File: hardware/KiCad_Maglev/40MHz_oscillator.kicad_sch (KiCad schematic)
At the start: 4 parts, among them Y2 IQXC-42_830108213209

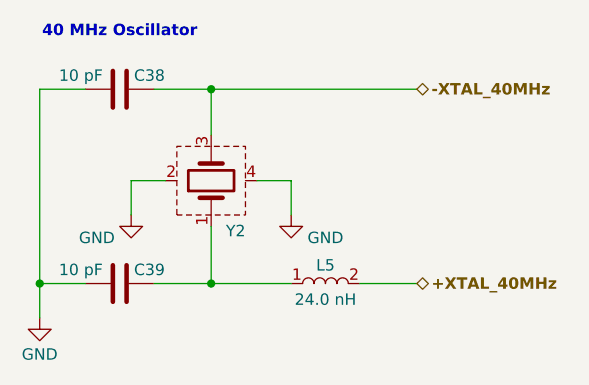
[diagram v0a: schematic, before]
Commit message: some changes to pcb schmatic, added datasheets for used components and linked wurth repo
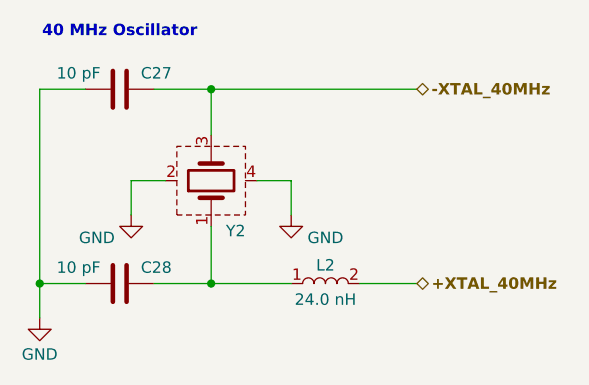
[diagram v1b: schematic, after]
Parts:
- removed C38, C39: 0402_885012005007, Capacitor_SMD_Wurth:C_Wurth_WCAP-CSGP-0402, symbol Capacitor_Wurth_WCAP-CSGP:0402_885012005007
- removed L5: 0402_744765124A, Inductor_SMD_Wurth:L_Wurth_WE-KI-0402, symbol Inductor_Wurth_WE-KI:0402_744765124A
- added C27, C28: 0603_R_885012006002, Capacitor_SMD_Wurth:C_Wurth_WCAP-CSGP-0603_R, symbol Capacitor_Wurth_WCAP-CSGP:0603_R_885012006002
- added L2: 0603_744761124A, Inductor_SMD_Wurth:L_Wurth_WE-KI-0603, symbol Inductor_Wurth_WE-KI:0603_744761124A
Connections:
- net +XTAL_40MHz: now also L2.2
- net -XTAL_40MHz: now also C27.2
- net GND: now also C27.1, C28.1
- net at Y2.1: now also C28.2, L2.1
